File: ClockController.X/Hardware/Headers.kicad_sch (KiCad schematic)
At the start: 8 parts, among them Q5 MMBT2222A-TP, Q6 MMBT2222A-TP

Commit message: Updated most footprints
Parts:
- DISP0: footprint Clock Controller:HDR-2X4 -> Connector_PinHeader_2.54mm:PinHeader_2x04_P2.54mm_Vertical
- OLED0: footprint Clock Controller:HDR-1X4 -> Connector_PinHeader_2.54mm:PinHeader_1x04_P2.54mm_Vertical
- Q5, Q6: footprint Clock Controller:SOT23-3P95_240X110L43X44N -> Package_TO_SOT_SMD:SOT-23
- R1, R2: footprint Clock Controller:RES_1206 -> Resistor_SMD:R_1206_3216Metric
- RCL0, RDA0: footprint Clock Controller:RES_0805 -> Resistor_SMD:R_0805_2012Metric
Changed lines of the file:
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@@
 			)
 		)
-		(property "Footprint" "Clock Controller:RES_0805"
+		(property "Footprint" "Resistor_SMD:R_0805_2012Metric"
 			(at 129.54 116.84 0)
 			(effects
@@
 			)
 		)
-		(property "Footprint" "Clock Controller:HDR-2X4"
+		(property "Footprint" "Connector_PinHeader_2.54mm:PinHeader_2x04_P2.54mm_Vertical"
 			(at 116.84 93.98 0)
 			(effects
@@
 			)
 		)
-		(property "Footprint" "Clock Controller:RES_0805"
+		(property "Footprint" "Resistor_SMD:R_0805_2012Metric"
 			(at 129.54 125.73 0)
 			(effects
@@
 			)
 		)
-		(property "Footprint" "Clock Controller:RES_1206"
+		(property "Footprint" "Resistor_SMD:R_1206_3216Metric"
 			(at 154.94 73.66 0)
 			(effects
@@
 			)
 		)
-		(property "Footprint" "Clock Controller:SOT23-3P95_240X110L43X44N"
+		(property "Footprint" "Package_TO_SOT_SMD:SOT-23"
 			(at 173.99 91.745 0)
 			(effects
@@
 			)
 		)
-		(property "Footprint" "Clock Controller:HDR-1X4"
+		(property "Footprint" "Connector_PinHeader_2.54mm:PinHeader_1x04_P2.54mm_Vertical"
 			(at 116.84 68.58 0)
 			(effects
@@
 			)
 		)
-		(property "Footprint" "Clock Controller:SOT23-3P95_240X110L43X44N"
+		(property "Footprint" "Package_TO_SOT_SMD:SOT-23"
 			(at 154.94 86.665 0)
 			(effects
@@
 			)
 		)
-		(property "Footprint" "Clock Controller:RES_1206"
+		(property "Footprint" "Resistor_SMD:R_1206_3216Metric"
 			(at 173.99 73.66 0)
 			(effects

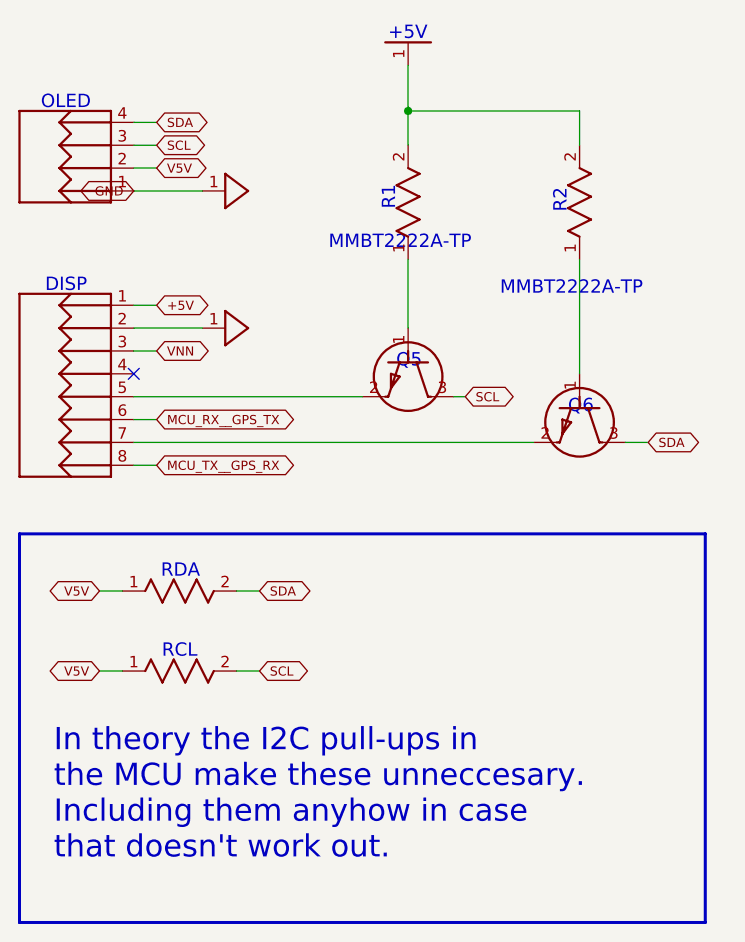
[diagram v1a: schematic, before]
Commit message: Deleted unused I2C pull-up resistors
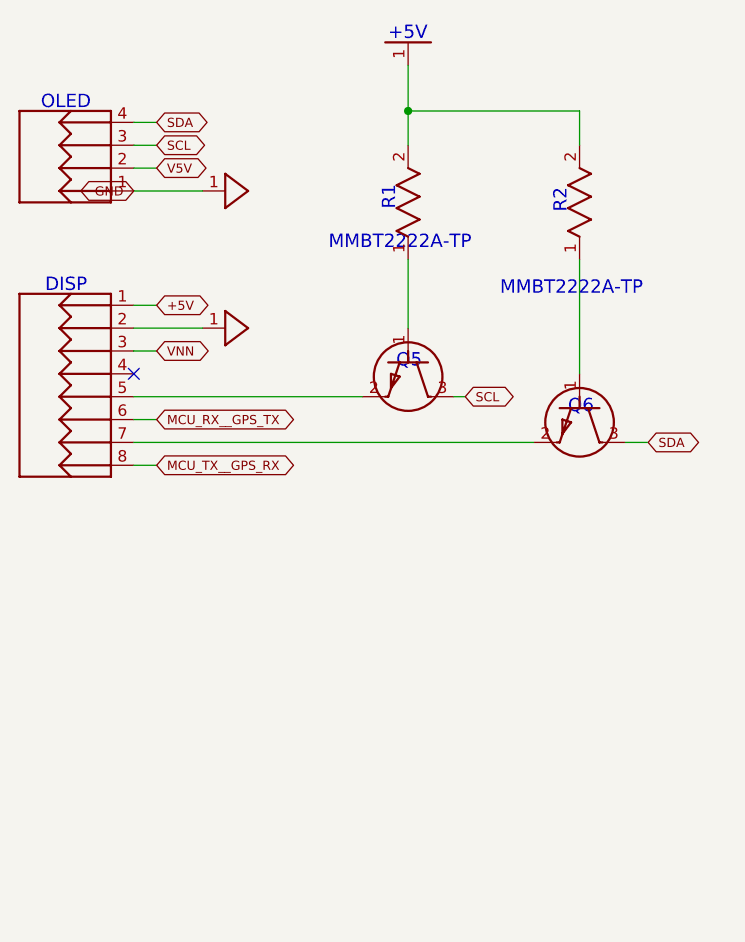
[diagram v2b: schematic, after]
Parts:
- removed RCL0, RDA0: 0, Resistor_SMD:R_0805_2012Metric, symbol Clock Controller-eagle-import:RES_0805
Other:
- note removed: "In theory the I2C pull-ups in the MCU make these unneccesary. Including them anyhow in case that doesn't work out."
- note removed: "RCL"
- note removed: "RDA"

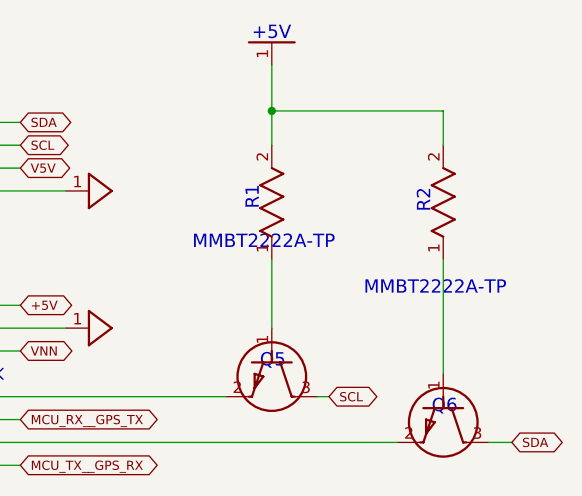
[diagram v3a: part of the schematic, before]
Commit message: Simplified I2C cutoff
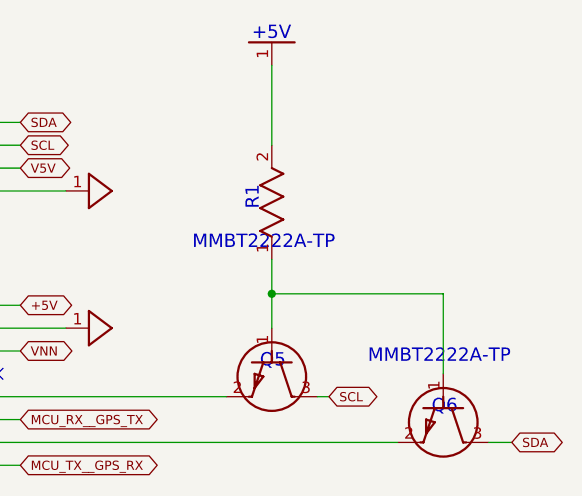
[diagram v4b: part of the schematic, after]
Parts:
- removed R2: 2.2k, Resistor_SMD:R_1206_3216Metric, symbol Clock Controller-eagle-import:RES_1206
- R1: footprint Resistor_SMD:R_1206_3216Metric -> Resistor_SMD:R_0603_1608Metric
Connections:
- net at Q5.1 (B), R1.1: now also Q6.1 (B)
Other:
- note removed: "R2"
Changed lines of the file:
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@@
 	(generator_version "9.0")
 	(paper "A4")
-	(text "R2"
-		(exclude_from_sim no)
-		(at 172.72 74.916 90)
+	(text "DISP"
+		(exclude_from_sim no)
+		(at 114.603 83.82 0)
 		(effects
 			(font
@@
 		)
 	)
-	(text "DISP"
-		(exclude_from_sim no)
-		(at 114.603 83.82 0)
+	(text "R1"
+		(exclude_from_sim no)
+		(at 153.67 74.589 90)
 		(effects
 			(font
@@
 		)
 	)
-	(text "R1"
-		(exclude_from_sim no)
-		(at 153.67 74.589 90)
+	(text "Q5"
+		(exclude_from_sim no)
+		(at 153.611 90.475 0)
 		(effects
 			(font
 				(size 1.48 1.48)
 			)
+			(justify left top)
+		)
+	)
+	(text "Q6"
+		(exclude_from_sim no)
+		(at 172.698 95.555 0)
+		(effects
+			(font
+				(size 1.48 1.48)
+			)
+			(justify left top)
+		)
+	)
+	(text "OLED"
+		(exclude_from_sim no)
+		(at 114.13 63.5 0)
+		(effects
+			(font
+				(size 1.48 1.48)
+			)
 			(justify left bottom)
 		)
 	)
-	(text "Q5"
-		(exclude_from_sim no)
-		(at 153.611 90.475 0)
+	(text "+5V"
+		(exclude_from_sim no)
+		(at 152.72 55.82 0)
 		(effects
 			(font
 				(size 1.48 1.48)
 			)
-			(justify left top)
-		)
-	)
-	(text "Q6"
-		(exclude_from_sim no)
-		(at 172.698 95.555 0)
+			(justify left bottom)
+		)
+	)
+	(text "MMBT2222A-TP"
+		(exclude_from_sim no)
+		(at 146.098 79.045 0)
 		(effects
 			(font
 				(size 1.48 1.48)
 			)
-			(justify left top)
-		)
-	)
-	(text "OLED"
-		(exclude_from_sim no)
-		(at 114.13 63.5 0)
+			(justify left bottom)
+		)
+	)
+	(text "MMBT2222A-TP"
+		(exclude_from_sim no)
+		(at 165.608 91.694 0)
 		(effects
 			(font
@@
 		)
 	)
-	(text "+5V"
-		(exclude_from_sim no)
-		(at 152.72 55.82 0)
-		(effects
-			(font
-				(size 1.48 1.48)
-			)
-			(justify left bottom)
-		)
-	)
-	(text "MMBT2222A-TP"
-		(exclude_from_sim no)
-		(at 146.098 79.045 0)
-		(effects
-			(font
-				(size 1.48 1.48)
-			)
-			(justify left bottom)
-		)
-	)
-	(text "MMBT2222A-TP"
-		(exclude_from_sim no)
-		(at 165.148 84.125 0)
-		(effects
-			(font
-				(size 1.48 1.48)
-			)
-			(justify left bottom)
-		)
-	)
 	(junction
-		(at 154.94 63.5)
+		(at 154.94 83.82)
 		(diameter 0)
 		(color 0 0 0 0)
@@
 	(wire
 		(pts
-			(xy 173.99 63.5) (xy 173.99 67.31)
-		)
-		(stroke
-			(width 0.25)
-			(type solid)
-		)
-	)
-	(wire
-		(pts
-			(xy 154.94 58.42) (xy 154.94 63.5)
+			(xy 154.94 58.42) (xy 154.94 67.31)
 		)
 		(stroke
@@
 	(wire
 		(pts
-			(xy 161.29 95.25) (xy 160.02 95.25)
+			(xy 154.94 83.82) (xy 154.94 87.63)
+		)
+		(stroke
+			(width 0.25)
+			(type solid)
+		)
+	)
+	(wire
+		(pts
+			(xy 173.99 92.71) (xy 173.99 83.82)
 		)
 		(stroke
@@
 	(wire
 		(pts
-			(xy 154.94 67.31) (xy 154.94 63.5)
-		)
-		(stroke
-			(width 0.25)
-			(type solid)
-		)
-	)
-	(wire
-		(pts
-			(xy 154.94 63.5) (xy 173.99 63.5)
-		)
-		(stroke
-			(width 0.25)
-			(type solid)
+			(xy 161.29 95.25) (xy 160.02 95.25)
+		)
+		(stroke
+			(width 0)
+			(type default)
 		)
 	)
@@
 	(wire
 		(pts
-			(xy 154.94 80.01) (xy 154.94 87.63)
+			(xy 154.94 80.01) (xy 154.94 83.82)
 		)
 		(stroke
@@
 	(wire
 		(pts
-			(xy 173.99 80.01) (xy 173.99 92.71)
-		)
-		(stroke
-			(width 0.25)
-			(type solid)
+			(xy 173.99 83.82) (xy 154.94 83.82)
+		)
+		(stroke
+			(width 0)
+			(type default)
 		)
 	)
@@
 			)
 		)
-		(property "Footprint" "Resistor_SMD:R_1206_3216Metric"
+		(property "Footprint" "Resistor_SMD:R_0603_1608Metric"
 			(at 154.94 73.66 0)
 			(effects
@@
 					(unit 1)
 				)
-			)
-		)
-	)
-	(symbol
-		(lib_id "Clock Controller-eagle-import:RES_1206")
-		(at 173.99 73.66 90)
-		(unit 1)
-		(exclude_from_sim no)
-		(in_bom yes)
-		(on_board yes)
-		(dnp no)
-		(property "Reference" "R2"
-			(at 173.99 73.66 0)
-			(effects
-				(font
-					(size 1.27 1.27)
-				)
-				(hide yes)
-			)
-		)
-		(property "Value" "2.2k"
-			(at 173.99 73.66 0)
-			(effects
-				(font
-					(size 1.27 1.27)
-				)
-				(hide yes)
-			)
-		)
-		(property "Footprint" "Resistor_SMD:R_1206_3216Metric"
-			(at 173.99 73.66 0)
-			(effects
-				(font
-					(size 1.27 1.27)
-				)
-				(hide yes)
-			)
-		)
-		(property "Datasheet" ""
-			(at 173.99 73.66 0)
-			(effects
-				(font
-					(size 1.27 1.27)
-				)
-				(hide yes)
-			)
-		)
-		(property "Description" ""
-			(at 173.99 73.66 0)
-			(effects
-				(font
-					(size 1.27 1.27)
-				)
-				(hide yes)
-			)
-		)
-		(pin "2"
-		)
-		(pin "1"
-		)
-		(instances
-			(project "Clock Controller"
-				(path "/de4049ea-1674-4dcc-86d3-bb1be3dcf2e7/f21bc6e7-c992-4316-9545-f3984eb63b0a"
-					(reference "R2")
-					(unit 1)
-				)

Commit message: Updated some footprints
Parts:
- OLED0: footprint Connector_PinHeader_2.54mm:PinHeader_1x04_P2.54mm_Vertical -> Display_:SSD1306 0.91 128x32 OLED
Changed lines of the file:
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@@
 			)
 		)
-		(property "Footprint" "Connector_PinHeader_2.54mm:PinHeader_1x04_P2.54mm_Vertical"
+		(property "Footprint" "Display_:SSD1306 0.91 128x32 OLED"
 			(at 116.84 68.58 0)
 			(effects

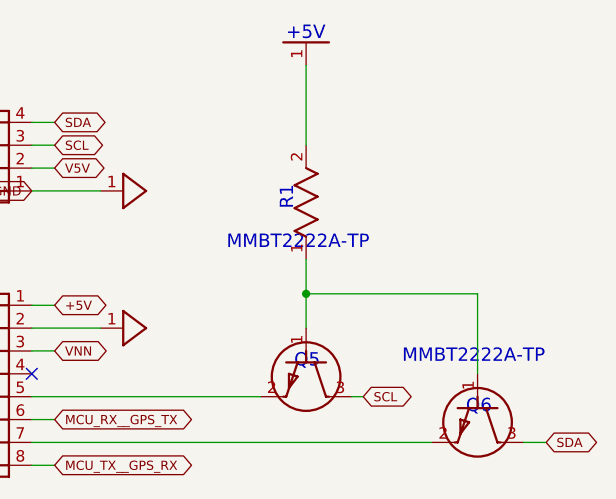
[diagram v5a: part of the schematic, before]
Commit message: Fixed bad pull-up design of I2C cutoff transistors
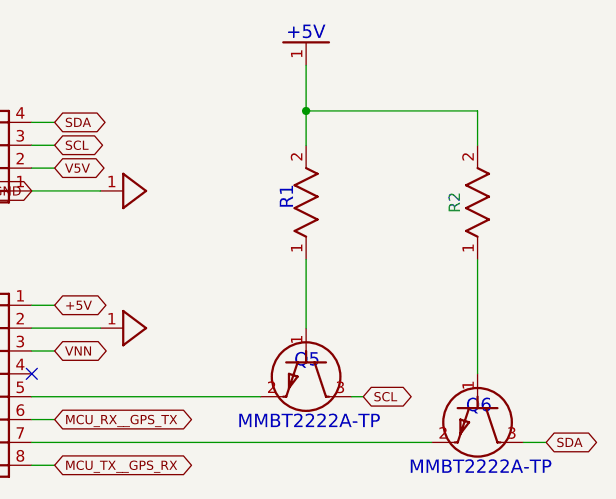
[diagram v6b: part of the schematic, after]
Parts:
- added R2: 2.2k, Resistor_SMD:R_0603_1608Metric, symbol Clock Controller-eagle-import:RES_1206
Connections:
- net +5V: now also R2.2
- net at Q5.1 (B), R1.1: no longer Q6.1 (B)
- new net: Q6.1 (B), R2.1
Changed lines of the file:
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@@
 	(text "MMBT2222A-TP"
 		(exclude_from_sim no)
-		(at 146.098 79.045 0)
+		(at 147.32 99.06 0)
 		(effects
 			(font
@@
 	(text "MMBT2222A-TP"
 		(exclude_from_sim no)
-		(at 165.608 91.694 0)
+		(at 166.37 104.14 0)
 		(effects
 			(font
@@
 	)
 	(junction
-		(at 154.94 83.82)
+		(at 154.94 63.5)
 		(diameter 0)
 		(color 0 0 0 0)
@@
 	(wire
 		(pts
-			(xy 154.94 58.42) (xy 154.94 67.31)
+			(xy 154.94 58.42) (xy 154.94 63.5)
 		)
 		(stroke
@@
 	(wire
 		(pts
-			(xy 154.94 83.82) (xy 154.94 87.63)
-		)
-		(stroke
-			(width 0.25)
-			(type solid)
-		)
-	)
-	(wire
-		(pts
-			(xy 173.99 92.71) (xy 173.99 83.82)
+			(xy 173.99 67.31) (xy 173.99 63.5)
+		)
+		(stroke
+			(width 0)
+			(type default)
+		)
+	)
+	(wire
+		(pts
+			(xy 173.99 80.01) (xy 173.99 92.71)
 		)
 		(stroke
@@
 	(wire
 		(pts
+			(xy 154.94 63.5) (xy 154.94 67.31)
+		)
+		(stroke
+			(width 0.25)
+			(type solid)
+		)
+	)
+	(wire
+		(pts
+			(xy 173.99 63.5) (xy 154.94 63.5)
+		)
+		(stroke
+			(width 0)
+			(type default)
+		)
+	)
+	(wire
+		(pts
 			(xy 124.46 64.77) (xy 127 64.77)
 		)
@@
 	(wire
 		(pts
-			(xy 154.94 80.01) (xy 154.94 83.82)
+			(xy 154.94 80.01) (xy 154.94 87.63)
 		)
 		(stroke
@@
 			(width 0.25)
 			(type solid)
-		)
-	)
-	(wire
-		(pts
-			(xy 173.99 83.82) (xy 154.94 83.82)
-		)
-		(stroke
-			(width 0)
-			(type default)
 		)
 	)
@@
 					(unit 1)
 				)
+			)
+		)
+	)
+	(symbol
+		(lib_id "Clock Controller-eagle-import:RES_1206")
+		(at 173.99 73.66 90)
+		(unit 1)
+		(exclude_from_sim no)
+		(in_bom yes)
+		(on_board yes)
+		(dnp no)
+		(property "Reference" "R2"
+			(at 171.45 73.66 0)
+			(effects
+				(font
+					(size 1.27 1.27)
+				)
+			)
+		)
+		(property "Value" "2.2k"
+			(at 173.99 73.66 0)
+			(effects
+				(font
+					(size 1.27 1.27)
+				)
+				(hide yes)
+			)
+		)
+		(property "Footprint" "Resistor_SMD:R_0603_1608Metric"
+			(at 173.99 73.66 0)
+			(effects
+				(font
+					(size 1.27 1.27)
+				)
+				(hide yes)
+			)
+		)
+		(property "Datasheet" ""
+			(at 173.99 73.66 0)
+			(effects
+				(font
+					(size 1.27 1.27)
+				)
+				(hide yes)
+			)
+		)
+		(property "Description" ""
+			(at 173.99 73.66 0)
+			(effects
+				(font
+					(size 1.27 1.27)
+				)
+				(hide yes)
+			)
+		)
+		(pin "2"
+		)
+		(pin "1"
+		)
+		(instances
+			(project "Clock Controller"
+				(path "/de4049ea-1674-4dcc-86d3-bb1be3dcf2e7/f21bc6e7-c992-4316-9545-f3984eb63b0a"
+					(reference "R2")
+					(unit 1)
+				)
